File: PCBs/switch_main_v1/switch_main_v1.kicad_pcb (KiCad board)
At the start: 2 copper layers, 15 parts, among them IC1001 TJA1055T_3_2Z, IC1101 MPQ5850GJ-AEC1-Z, J1101 76825-0004, J901 TMJG46945AENL, U1101 TVS2701DRBR, U201 SJA1105QELY, U301 STM32H573RIVx, U401 LT8692SIV-PBF, U402 TPS16416DRCR, U403 LMR34206SC5QRNXRQ1, U501 DP83867CSRGZR, U601 DP83867CSRGZR, U701 DP83867CSRGZR, U801 DP83867CSRGZR

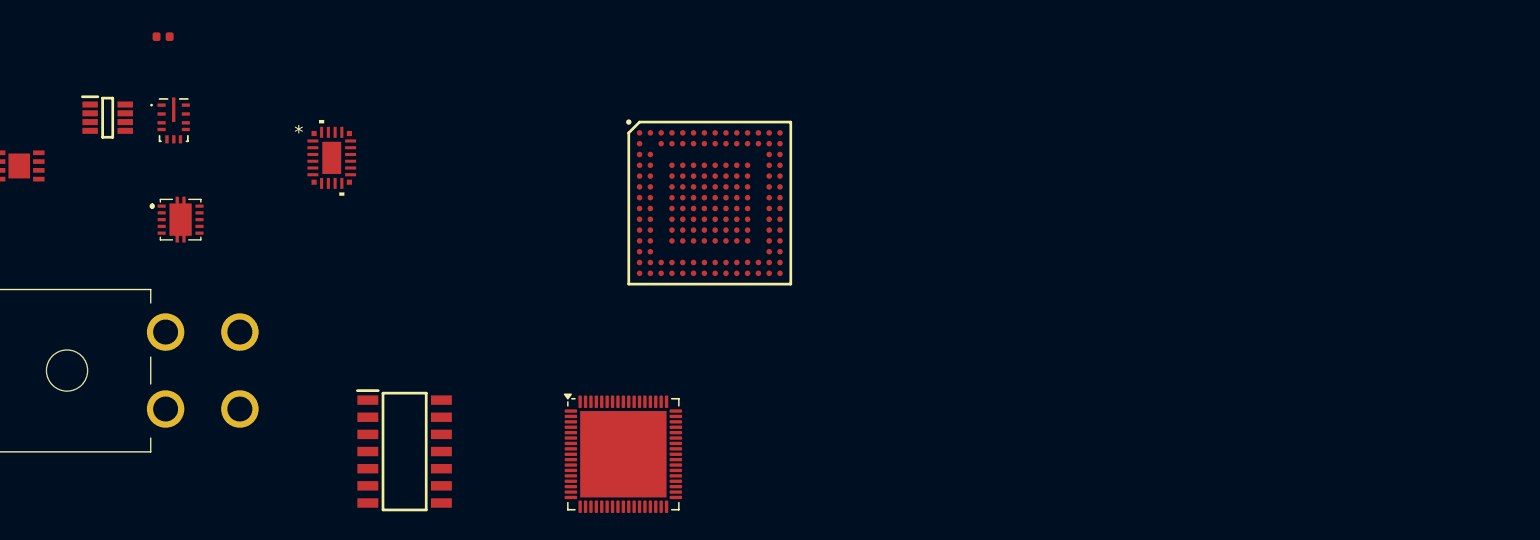
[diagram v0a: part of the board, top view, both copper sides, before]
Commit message: Connectors schematic almost complete
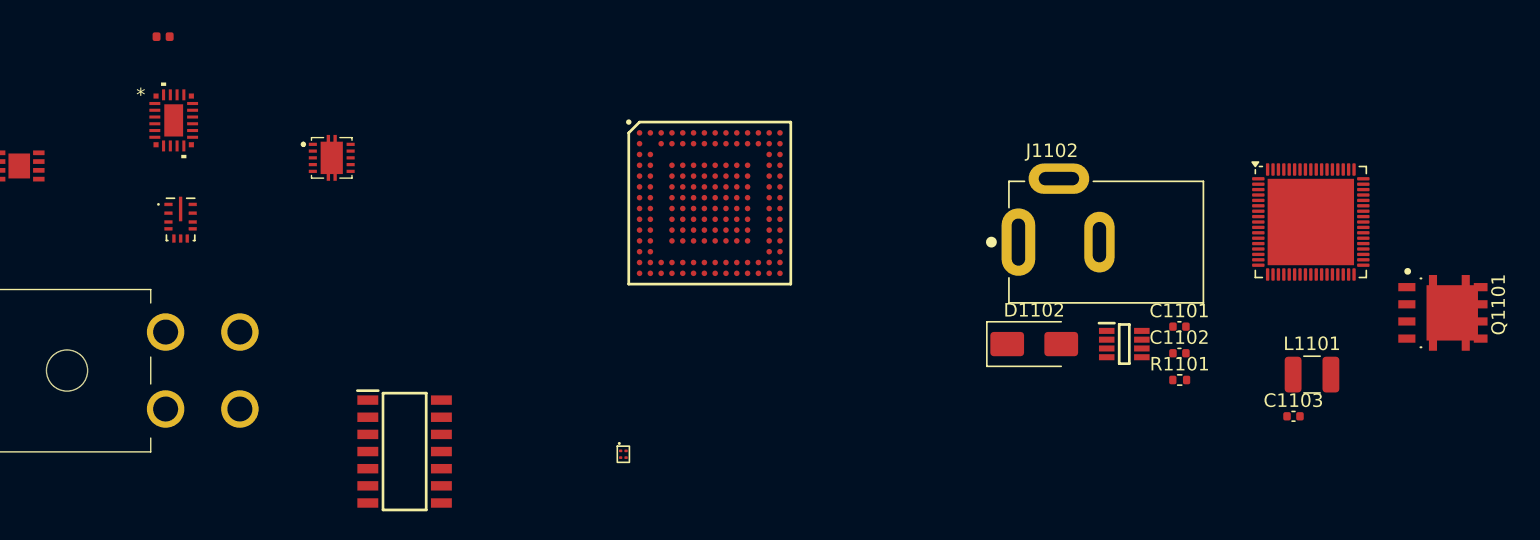
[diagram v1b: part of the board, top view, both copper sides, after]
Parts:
- removed IC1101: MPQ5850GJ-AEC1-Z, switch_footprints:SOT65P280X100-8N
- added C1101: 1u, Capacitor_SMD:C_0402_1005Metric, F.Cu at (206.4, 119.8)
- added C1102: 4u7, Capacitor_SMD:C_0402_1005Metric, F.Cu at (206.4, 121.7)
- added C1103: 10n, Capacitor_SMD:C_0402_1005Metric, F.Cu at (214.8, 126.4)
- added D1102: SK14, Diode_SMD:D_SMA, F.Cu at (195.6, 121.0)
- added J1102: PJ-002AH, switch_footprints:CUI_PJ-002AH, F.Cu at (194.5, 113.5)
- added L1101: BRL3225T680K, Inductor_SMD:L_1210_3225Metric, F.Cu at (216.2, 123.3)
- added Q1101: DMTH6016LPSQ-13, switch_footprints:Diodes_Incorporated-PowerDI5060-8-03_2017-0-MFG, F.Cu at (225.9, 118.7)
- added R1101: 100k, Resistor_SMD:R_0402_1005Metric, F.Cu at (206.4, 123.7)
- added U1102: MPQ5850GJ-AEC1-Z, switch_footprints:SOT65P280X100-8N, F.Cu at (202.3, 121.0)
- added U302: STM32H573RIVx, switch_footprints:QFN-68-1EP_8x8mm_P0.4mm_EP6.4x6.4mm, F.Cu at (216.1, 112.0)
- U301: value STM32H573RIVx -> M24256X-FCU6T_VF; footprint switch_footprints:QFN-68-1EP_8x8mm_P0.4mm_EP6.4x6.4mm -> switch_footprints:BGA4C50P2X2_70X98X33
- U401: value LT8692SIV-PBF -> TPS16416DRCR; footprint switch_footprints:LT8692SIV_PBF -> switch_footprints:TPS74901DRCR
- U402: value TPS16416DRCR -> LMR34206SC5QRNXRQ1; footprint switch_footprints:TPS74901DRCR -> switch_footprints:CONV_LMR33620BRNXT
- U403: value LMR34206SC5QRNXRQ1 -> LT8692SIV-PBF; footprint switch_footprints:CONV_LMR33620BRNXT -> switch_footprints:LT8692SIV_PBF
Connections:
- D1101 pad 2: VDC -> /Connectors/VIN_RAW
- J1101 pad 1: unconnected-(J1101-CANH-Pad1) -> /Connectors/CAN.CANH
- J1101 pad 2: unconnected-(J1101-CANL-Pad2) -> /Connectors/CAN.CANL
- J1101 pad 3: unconnected-(J1101-VSYS-Pad3) -> /Connectors/VIN_RAW
- J1101 pad 4: unconnected-(J1101-GND-Pad4) -> GND
- U1101 pad 1: VDC -> /Connectors/VIN_RAW
- U1101 pad 2: VDC -> /Connectors/VIN_RAW
- U1101 pad 3: VDC -> /Connectors/VIN_RAW
- U1101 pad 4: VDC -> /Connectors/VIN_RAW

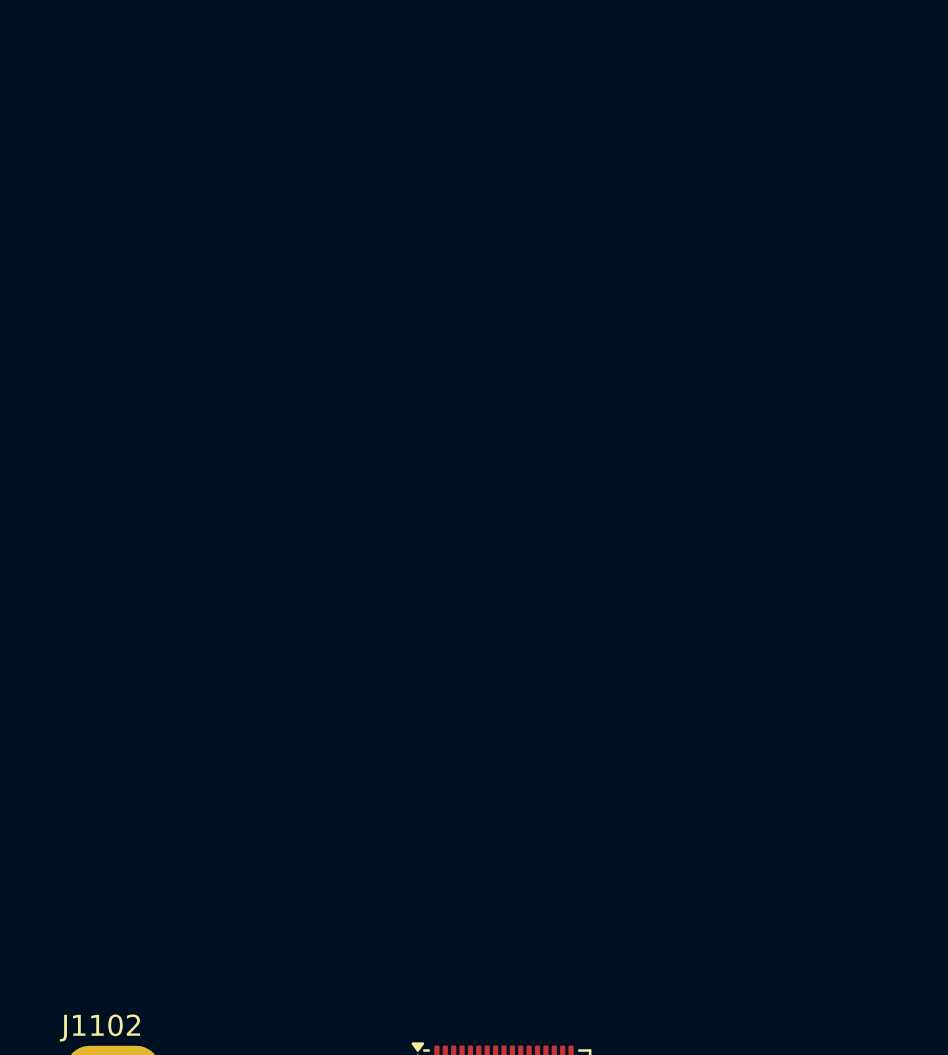
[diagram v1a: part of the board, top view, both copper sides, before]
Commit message: Block diagram layout change
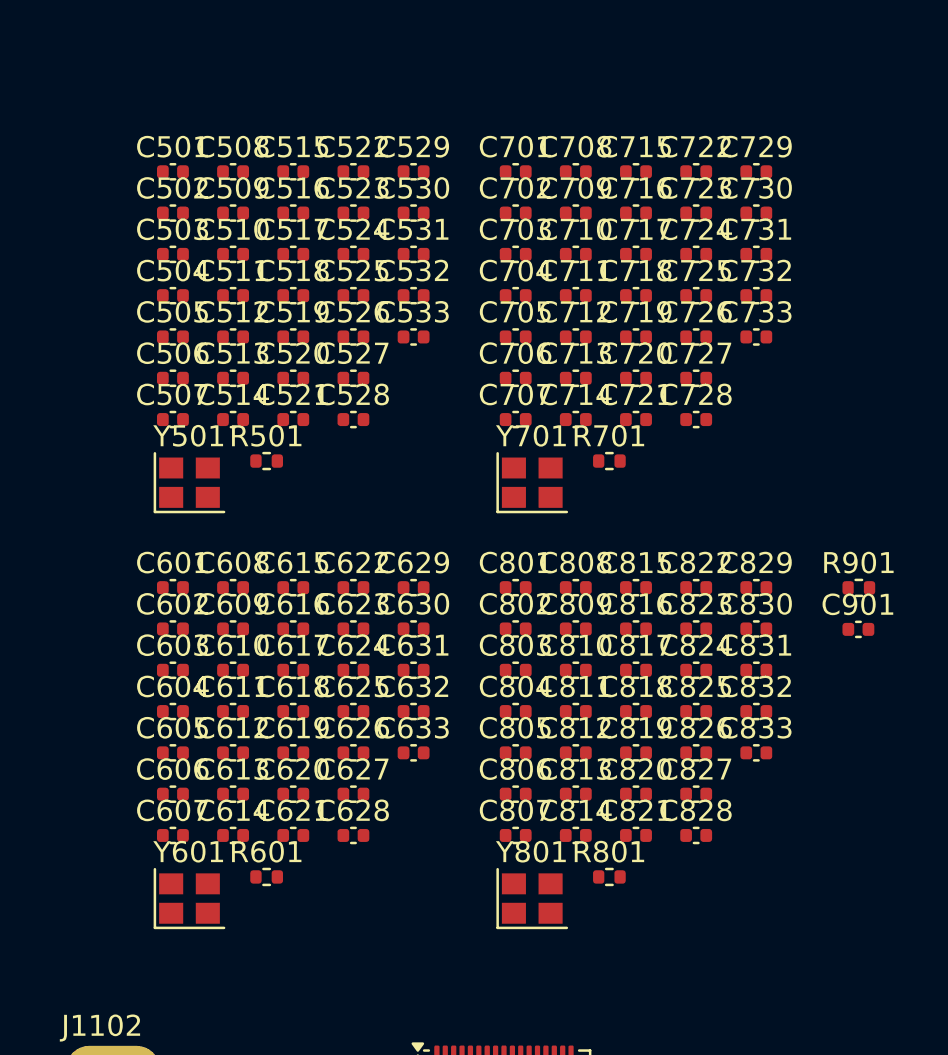
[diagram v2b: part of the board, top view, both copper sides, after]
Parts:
- added C501: 100n, Capacitor_SMD:C_0402_1005Metric, F.Cu at (200.3, 66.0)
- added C502: 100n, Capacitor_SMD:C_0402_1005Metric, F.Cu at (200.3, 67.9)
- added C503: 27p, Capacitor_SMD:C_0402_1005Metric, F.Cu at (200.3, 69.9)
- added C504: 27p, Capacitor_SMD:C_0402_1005Metric, F.Cu at (200.3, 71.9)
- added C505: 27p, Capacitor_SMD:C_0402_1005Metric, F.Cu at (200.3, 73.8)
- added C506: 100n, Capacitor_SMD:C_0402_1005Metric, F.Cu at (200.3, 75.8)
- added C507: 100n, Capacitor_SMD:C_0402_1005Metric, F.Cu at (200.3, 77.8)
- added C508: 100n, Capacitor_SMD:C_0402_1005Metric, F.Cu at (203.2, 66.0)
- added C509: 1u, Capacitor_SMD:C_0402_1005Metric, F.Cu at (203.2, 67.9)
- added C510: 1u, Capacitor_SMD:C_0402_1005Metric, F.Cu at (203.2, 69.9)
- added C511: 1u, Capacitor_SMD:C_0402_1005Metric, F.Cu at (203.2, 71.9)
- added C512: 1u, Capacitor_SMD:C_0402_1005Metric, F.Cu at (203.2, 73.8)
- added C513: 1u, Capacitor_SMD:C_0402_1005Metric, F.Cu at (203.2, 75.8)
- added C514: 10n, Capacitor_SMD:C_0402_1005Metric, F.Cu at (203.2, 77.8)
- added C515: 10u, Capacitor_SMD:C_0402_1005Metric, F.Cu at (206.1, 66.0)
- added C516: 10n, Capacitor_SMD:C_0402_1005Metric, F.Cu at (206.1, 67.9)
- added C517: 10u, Capacitor_SMD:C_0402_1005Metric, F.Cu at (206.1, 69.9)
- added C518: 10n, Capacitor_SMD:C_0402_1005Metric, F.Cu at (206.1, 71.9)
- added C519: 100n, Capacitor_SMD:C_0402_1005Metric, F.Cu at (206.1, 73.8)
- added C520: 100n, Capacitor_SMD:C_0402_1005Metric, F.Cu at (206.1, 75.8)
- added C521: 1u, Capacitor_SMD:C_0402_1005Metric, F.Cu at (206.1, 77.8)
- added C522: 1u, Capacitor_SMD:C_0402_1005Metric, F.Cu at (208.9, 66.0)
- added C523: 10u, Capacitor_SMD:C_0402_1005Metric, F.Cu at (208.9, 67.9)
- added C524: 10n, Capacitor_SMD:C_0402_1005Metric, F.Cu at (208.9, 69.9)
- added C525: 100n, Capacitor_SMD:C_0402_1005Metric, F.Cu at (208.9, 71.9)
- added C526: 100n, Capacitor_SMD:C_0402_1005Metric, F.Cu at (208.9, 73.8)
- added C527: 100n, Capacitor_SMD:C_0402_1005Metric, F.Cu at (208.9, 75.8)
- added C528: 1u, Capacitor_SMD:C_0402_1005Metric, F.Cu at (208.9, 77.8)
- added C529: 1u, Capacitor_SMD:C_0402_1005Metric, F.Cu at (211.8, 66.0)
- added C530: 1u, Capacitor_SMD:C_0402_1005Metric, F.Cu at (211.8, 67.9)
- added C531: 10u, Capacitor_SMD:C_0402_1005Metric, F.Cu at (211.8, 69.9)
- added C532: 100n, Capacitor_SMD:C_0402_1005Metric, F.Cu at (211.8, 71.9)
- added C533: 1u, Capacitor_SMD:C_0402_1005Metric, F.Cu at (211.8, 73.8)
- added C601: 100n, Capacitor_SMD:C_0402_1005Metric, F.Cu at (200.3, 85.8)
- added C602: 100n, Capacitor_SMD:C_0402_1005Metric, F.Cu at (200.3, 87.8)
- added C603: 27p, Capacitor_SMD:C_0402_1005Metric, F.Cu at (200.3, 89.8)
- added C604: 27p, Capacitor_SMD:C_0402_1005Metric, F.Cu at (200.3, 91.7)
- added C605: 27p, Capacitor_SMD:C_0402_1005Metric, F.Cu at (200.3, 93.7)
- added C606: 100n, Capacitor_SMD:C_0402_1005Metric, F.Cu at (200.3, 95.7)
- added C607: 100n, Capacitor_SMD:C_0402_1005Metric, F.Cu at (200.3, 97.6)
- added C608: 100n, Capacitor_SMD:C_0402_1005Metric, F.Cu at (203.2, 85.8)
- added C609: 1u, Capacitor_SMD:C_0402_1005Metric, F.Cu at (203.2, 87.8)
- added C610: 1u, Capacitor_SMD:C_0402_1005Metric, F.Cu at (203.2, 89.8)
- added C611: 1u, Capacitor_SMD:C_0402_1005Metric, F.Cu at (203.2, 91.7)
- added C612: 1u, Capacitor_SMD:C_0402_1005Metric, F.Cu at (203.2, 93.7)
- added C613: 1u, Capacitor_SMD:C_0402_1005Metric, F.Cu at (203.2, 95.7)
- added C614: 10n, Capacitor_SMD:C_0402_1005Metric, F.Cu at (203.2, 97.6)
- added C615: 10u, Capacitor_SMD:C_0402_1005Metric, F.Cu at (206.1, 85.8)
- added C616: 10n, Capacitor_SMD:C_0402_1005Metric, F.Cu at (206.1, 87.8)
- added C617: 10u, Capacitor_SMD:C_0402_1005Metric, F.Cu at (206.1, 89.8)
- added C618: 10n, Capacitor_SMD:C_0402_1005Metric, F.Cu at (206.1, 91.7)
- added C619: 100n, Capacitor_SMD:C_0402_1005Metric, F.Cu at (206.1, 93.7)
- added C620: 100n, Capacitor_SMD:C_0402_1005Metric, F.Cu at (206.1, 95.7)
- added C621: 1u, Capacitor_SMD:C_0402_1005Metric, F.Cu at (206.1, 97.6)
- added C622: 1u, Capacitor_SMD:C_0402_1005Metric, F.Cu at (208.9, 85.8)
- added C623: 10u, Capacitor_SMD:C_0402_1005Metric, F.Cu at (208.9, 87.8)
- added C624: 10n, Capacitor_SMD:C_0402_1005Metric, F.Cu at (208.9, 89.8)
- added C625: 100n, Capacitor_SMD:C_0402_1005Metric, F.Cu at (208.9, 91.7)
- added C626: 100n, Capacitor_SMD:C_0402_1005Metric, F.Cu at (208.9, 93.7)
- added C627: 100n, Capacitor_SMD:C_0402_1005Metric, F.Cu at (208.9, 95.7)
- added C628: 1u, Capacitor_SMD:C_0402_1005Metric, F.Cu at (208.9, 97.6)
- added C629: 1u, Capacitor_SMD:C_0402_1005Metric, F.Cu at (211.8, 85.8)
- added C630: 1u, Capacitor_SMD:C_0402_1005Metric, F.Cu at (211.8, 87.8)
- added C631: 10u, Capacitor_SMD:C_0402_1005Metric, F.Cu at (211.8, 89.8)
- added C632: 100n, Capacitor_SMD:C_0402_1005Metric, F.Cu at (211.8, 91.7)
- added C633: 1u, Capacitor_SMD:C_0402_1005Metric, F.Cu at (211.8, 93.7)
- added C701: 100n, Capacitor_SMD:C_0402_1005Metric, F.Cu at (216.7, 66.0)
- added C702: 100n, Capacitor_SMD:C_0402_1005Metric, F.Cu at (216.7, 67.9)
- added C703: 27p, Capacitor_SMD:C_0402_1005Metric, F.Cu at (216.7, 69.9)
- added C704: 27p, Capacitor_SMD:C_0402_1005Metric, F.Cu at (216.7, 71.9)
- added C705: 27p, Capacitor_SMD:C_0402_1005Metric, F.Cu at (216.7, 73.8)
- added C706: 100n, Capacitor_SMD:C_0402_1005Metric, F.Cu at (216.7, 75.8)
- added C707: 100n, Capacitor_SMD:C_0402_1005Metric, F.Cu at (216.7, 77.8)
- added C708: 100n, Capacitor_SMD:C_0402_1005Metric, F.Cu at (219.5, 66.0)
- added C709: 1u, Capacitor_SMD:C_0402_1005Metric, F.Cu at (219.5, 67.9)
- added C710: 1u, Capacitor_SMD:C_0402_1005Metric, F.Cu at (219.5, 69.9)
- added C711: 1u, Capacitor_SMD:C_0402_1005Metric, F.Cu at (219.5, 71.9)
- added C712: 1u, Capacitor_SMD:C_0402_1005Metric, F.Cu at (219.5, 73.8)
- added C713: 1u, Capacitor_SMD:C_0402_1005Metric, F.Cu at (219.5, 75.8)
- added C714: 10n, Capacitor_SMD:C_0402_1005Metric, F.Cu at (219.5, 77.8)
- added C715: 10u, Capacitor_SMD:C_0402_1005Metric, F.Cu at (222.4, 66.0)
- added C716: 10n, Capacitor_SMD:C_0402_1005Metric, F.Cu at (222.4, 67.9)
- added C717: 10u, Capacitor_SMD:C_0402_1005Metric, F.Cu at (222.4, 69.9)
- added C718: 10n, Capacitor_SMD:C_0402_1005Metric, F.Cu at (222.4, 71.9)
- added C719: 100n, Capacitor_SMD:C_0402_1005Metric, F.Cu at (222.4, 73.8)
- added C720: 100n, Capacitor_SMD:C_0402_1005Metric, F.Cu at (222.4, 75.8)
- added C721: 1u, Capacitor_SMD:C_0402_1005Metric, F.Cu at (222.4, 77.8)
- added C722: 1u, Capacitor_SMD:C_0402_1005Metric, F.Cu at (225.3, 66.0)
- added C723: 10u, Capacitor_SMD:C_0402_1005Metric, F.Cu at (225.3, 67.9)
- added C724: 10n, Capacitor_SMD:C_0402_1005Metric, F.Cu at (225.3, 69.9)
- added C725: 100n, Capacitor_SMD:C_0402_1005Metric, F.Cu at (225.3, 71.9)
- added C726: 100n, Capacitor_SMD:C_0402_1005Metric, F.Cu at (225.3, 73.8)
- added C727: 100n, Capacitor_SMD:C_0402_1005Metric, F.Cu at (225.3, 75.8)
- added C728: 1u, Capacitor_SMD:C_0402_1005Metric, F.Cu at (225.3, 77.8)
- added C729: 1u, Capacitor_SMD:C_0402_1005Metric, F.Cu at (228.2, 66.0)
- added C730: 1u, Capacitor_SMD:C_0402_1005Metric, F.Cu at (228.2, 67.9)
- added C731: 10u, Capacitor_SMD:C_0402_1005Metric, F.Cu at (228.2, 69.9)
- added C732: 100n, Capacitor_SMD:C_0402_1005Metric, F.Cu at (228.2, 71.9)
- added C733: 1u, Capacitor_SMD:C_0402_1005Metric, F.Cu at (228.2, 73.8)
- added C801: 100n, Capacitor_SMD:C_0402_1005Metric, F.Cu at (216.7, 85.8)
- added C802: 100n, Capacitor_SMD:C_0402_1005Metric, F.Cu at (216.7, 87.8)
- added C803: 27p, Capacitor_SMD:C_0402_1005Metric, F.Cu at (216.7, 89.8)
- added C804: 27p, Capacitor_SMD:C_0402_1005Metric, F.Cu at (216.7, 91.7)
- added C805: 27p, Capacitor_SMD:C_0402_1005Metric, F.Cu at (216.7, 93.7)
- added C806: 100n, Capacitor_SMD:C_0402_1005Metric, F.Cu at (216.7, 95.7)
- added C807: 100n, Capacitor_SMD:C_0402_1005Metric, F.Cu at (216.7, 97.6)
- added C808: 100n, Capacitor_SMD:C_0402_1005Metric, F.Cu at (219.5, 85.8)
- added C809: 1u, Capacitor_SMD:C_0402_1005Metric, F.Cu at (219.5, 87.8)
- added C810: 1u, Capacitor_SMD:C_0402_1005Metric, F.Cu at (219.5, 89.8)
- added C811: 1u, Capacitor_SMD:C_0402_1005Metric, F.Cu at (219.5, 91.7)
- added C812: 1u, Capacitor_SMD:C_0402_1005Metric, F.Cu at (219.5, 93.7)
- added C813: 1u, Capacitor_SMD:C_0402_1005Metric, F.Cu at (219.5, 95.7)
- added C814: 10n, Capacitor_SMD:C_0402_1005Metric, F.Cu at (219.5, 97.6)
- added C815: 10u, Capacitor_SMD:C_0402_1005Metric, F.Cu at (222.4, 85.8)
- added C816: 10n, Capacitor_SMD:C_0402_1005Metric, F.Cu at (222.4, 87.8)
- added C817: 10u, Capacitor_SMD:C_0402_1005Metric, F.Cu at (222.4, 89.8)
- added C818: 10n, Capacitor_SMD:C_0402_1005Metric, F.Cu at (222.4, 91.7)
- added C819: 100n, Capacitor_SMD:C_0402_1005Metric, F.Cu at (222.4, 93.7)
- added C820: 100n, Capacitor_SMD:C_0402_1005Metric, F.Cu at (222.4, 95.7)
- added C821: 1u, Capacitor_SMD:C_0402_1005Metric, F.Cu at (222.4, 97.6)
- added C822: 1u, Capacitor_SMD:C_0402_1005Metric, F.Cu at (225.3, 85.8)
- added C823: 10u, Capacitor_SMD:C_0402_1005Metric, F.Cu at (225.3, 87.8)
- added C824: 10n, Capacitor_SMD:C_0402_1005Metric, F.Cu at (225.3, 89.8)
- added C825: 100n, Capacitor_SMD:C_0402_1005Metric, F.Cu at (225.3, 91.7)
- added C826: 100n, Capacitor_SMD:C_0402_1005Metric, F.Cu at (225.3, 93.7)
- added C827: 100n, Capacitor_SMD:C_0402_1005Metric, F.Cu at (225.3, 95.7)
- added C828: 1u, Capacitor_SMD:C_0402_1005Metric, F.Cu at (225.3, 97.6)
- added C829: 1u, Capacitor_SMD:C_0402_1005Metric, F.Cu at (228.2, 85.8)
- added C830: 1u, Capacitor_SMD:C_0402_1005Metric, F.Cu at (228.2, 87.8)
- added C831: 10u, Capacitor_SMD:C_0402_1005Metric, F.Cu at (228.2, 89.8)
- added C832: 100n, Capacitor_SMD:C_0402_1005Metric, F.Cu at (228.2, 91.7)
- added C833: 1u, Capacitor_SMD:C_0402_1005Metric, F.Cu at (228.2, 93.7)
- added C901: C_Small, Capacitor_SMD:C_0402_1005Metric, F.Cu at (233.0, 87.8)
- added R501: 11k, Resistor_SMD:R_0402_1005Metric, F.Cu at (204.8, 79.8)
- added R601: 11k, Resistor_SMD:R_0402_1005Metric, F.Cu at (204.8, 99.6)
- added R701: 11k, Resistor_SMD:R_0402_1005Metric, F.Cu at (221.1, 79.8)
- added R801: 11k, Resistor_SMD:R_0402_1005Metric, F.Cu at (221.1, 99.6)
- added R901: R_Small, Resistor_SMD:R_0402_1005Metric, F.Cu at (233.0, 85.8)
- added Y501: ECS-250-18-36B2-CTY-TR, Crystal:Crystal_SMD_2520-4Pin_2.5x2.0mm, F.Cu at (201.1, 80.8)
- added Y601: ECS-250-18-36B2-CTY-TR, Crystal:Crystal_SMD_2520-4Pin_2.5x2.0mm, F.Cu at (201.1, 100.6)
- added Y701: ECS-250-18-36B2-CTY-TR, Crystal:Crystal_SMD_2520-4Pin_2.5x2.0mm, F.Cu at (217.5, 80.8)
- added Y801: ECS-250-18-36B2-CTY-TR, Crystal:Crystal_SMD_2520-4Pin_2.5x2.0mm, F.Cu at (217.5, 100.6)
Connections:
- J901 pad 15: GND -> Earth
- J901 pad 16: GND -> Earth
- J901 pad 17: GND -> Earth
- J901 pad 18: GND -> Earth
- J901 pad 19: GND -> Earth
- J901 pad 2A: unconnected-(J901-TD1+-Pad2A) -> /ETHERNET_1.TD0_P
- J901 pad 2B: unconnected-(J901-TD1+-Pad2B) -> /ETHERNET_2.TD0_P
- J901 pad 2C: unconnected-(J901-TD1+-Pad2C) -> /ETHERNET_3.TD0_P
- J901 pad 2D: unconnected-(J901-TD1+-Pad2D) -> /ETHERNET_4.TD0_P
- J901 pad 3A: unconnected-(J901-TD1--Pad3A) -> /ETHERNET_1.TD0_N
- J901 pad 3B: unconnected-(J901-TD1--Pad3B) -> /ETHERNET_2.TD0_N
- J901 pad 3C: unconnected-(J901-TD1--Pad3C) -> /ETHERNET_3.TD0_N
- J901 pad 3D: unconnected-(J901-TD1--Pad3D) -> /ETHERNET_4.TD0_N
- J901 pad 4A: unconnected-(J901-TD2+-Pad4A) -> /ETHERNET_1.TD1_P
- J901 pad 4B: unconnected-(J901-TD2+-Pad4B) -> /ETHERNET_2.TD1_P
- J901 pad 4C: unconnected-(J901-TD2+-Pad4C) -> /ETHERNET_3.TD1_P
- J901 pad 4D: unconnected-(J901-TD2+-Pad4D) -> /ETHERNET_4.TD1_P
- J901 pad 5A: unconnected-(J901-TD2--Pad5A) -> /ETHERNET_1.TD1_N
- J901 pad 5B: unconnected-(J901-TD2--Pad5B) -> /ETHERNET_2.TD1_N
- J901 pad 5C: unconnected-(J901-TD2--Pad5C) -> /ETHERNET_3.TD1_N
- J901 pad 5D: unconnected-(J901-TD2--Pad5D) -> /ETHERNET_4.TD1_N
- J901 pad 6A: unconnected-(J901-TD3+-Pad6A) -> /ETHERNET_1.TD2_P
- J901 pad 6B: unconnected-(J901-TD3+-Pad6B) -> /ETHERNET_2.TD2_P
- J901 pad 6C: unconnected-(J901-TD3+-Pad6C) -> /ETHERNET_3.TD2_P
- J901 pad 6D: unconnected-(J901-TD3+-Pad6D) -> /ETHERNET_4.TD2_P
- J901 pad 7A: unconnected-(J901-TD3--Pad7A) -> /ETHERNET_1.TD2_N
- J901 pad 7B: unconnected-(J901-TD3--Pad7B) -> /ETHERNET_2.TD2_N
- J901 pad 7C: unconnected-(J901-TD3--Pad7C) -> /ETHERNET_3.TD2_N
- J901 pad 7D: unconnected-(J901-TD3--Pad7D) -> /ETHERNET_4.TD2_N
- J901 pad 8A: unconnected-(J901-TD4+-Pad8A) -> /ETHERNET_1.TD3_P
- J901 pad 8B: unconnected-(J901-TD4+-Pad8B) -> /ETHERNET_2.TD3_P
- J901 pad 8C: unconnected-(J901-TD4+-Pad8C) -> /ETHERNET_3.TD3_P
- J901 pad 8D: unconnected-(J901-TD4+-Pad8D) -> /ETHERNET_4.TD3_P
- J901 pad 9A: unconnected-(J901-TD4--Pad9A) -> /ETHERNET_1.TD3_N
- J901 pad 9B: unconnected-(J901-TD4--Pad9B) -> /ETHERNET_2.TD3_N
- J901 pad 9C: unconnected-(J901-TD4--Pad9C) -> /ETHERNET_3.TD3_N
- J901 pad 9D: unconnected-(J901-TD4--Pad9D) -> /ETHERNET_4.TD3_N
- U201 pad A11: unconnected-(U201A-MII2_RX_DV/CRS_DV/RX_CTL-PadA11) -> /RGMII_2.RX_CTRL
- U201 pad A12: unconnected-(U201A-MII2_RXD2-PadA12) -> /RGMII_2.RX_D2
- U201 pad A13: unconnected-(U201A-MII2_RXD0-PadA13) -> /RGMII_2.RX_D0
- U201 pad A2: unconnected-(U201A-MII0_TXD0-PadA2) -> /RGMII_0.TX_D0
- U201 pad A4: unconnected-(U201A-MII1_RX_DV/CRS_DV/RX_CTL-PadA4) -> /RGMII_1.RX_CTRL
- U201 pad A5: unconnected-(U201A-MII1_RXD2-PadA5) -> /RGMII_1.RX_D2
- U201 pad A6: unconnected-(U201A-MII1_RXD0-PadA6) -> /RGMII_1.RX_D0
- U201 pad A7: unconnected-(U201A-MII1_TX_CLK/REF_CLK/TXC-PadA7) -> /RGMII_1.TX_CLK
- U201 pad A8: unconnected-(U201A-MII1_TXD3-PadA8) -> /RGMII_1.TX_D3
- U201 pad A9: unconnected-(U201A-MII1_TXD1-PadA9) -> /RGMII_1.TX_D1
- U201 pad B1: unconnected-(U201A-MII0_TXD1-PadB1) -> /RGMII_0.TX_D1
- U201 pad B10: unconnected-(U201A-MII2_RX_ER-PadB10) -> GND
- U201 pad B11: unconnected-(U201A-MII2_RXD3-PadB11) -> /RGMII_2.RX_D3
- U201 pad B12: unconnected-(U201A-MII2_RXD1-PadB12) -> /RGMII_2.RX_D1
- U201 pad B14: unconnected-(U201A-MII2_RX_CLK/RXC-PadB14) -> /RGMII_2.RX_CLK
- U201 pad B3: unconnected-(U201A-MII1_RX_ER-PadB3) -> GND
- U201 pad B4: unconnected-(U201A-MII1_RXD3-PadB4) -> /RGMII_1.RX_D3
- U201 pad B5: unconnected-(U201A-MII1_RXD1-PadB5) -> /RGMII_1.RX_D1
- U201 pad B6: unconnected-(U201A-MII1_RX_CLK/RXC-PadB6) -> /RGMII_1.RX_CLK
- U201 pad B7: unconnected-(U201A-MII1_TTX_EN/TX_CTL-PadB7) -> /RGMII_1.TX_CTRL
- U201 pad B8: unconnected-(U201A-MII1_TXD2-PadB8) -> /RGMII_1.TX_D2
- U201 pad B9: unconnected-(U201A-MII1_TXD0-PadB9) -> /RGMII_1.TX_D0
- U201 pad C1: unconnected-(U201A-MII0_TXD3-PadC1) -> /RGMII_0.TX_D3
- U201 pad C13: unconnected-(U201A-MII2_TX_EN/TX_CTL-PadC13) -> /RGMII_2.TX_CTRL
- U201 pad C14: unconnected-(U201A-MII2_TX_CLK/REF_CLK/TXC-PadC14) -> /RGMII_2.TX_CLK
- U201 pad C2: unconnected-(U201A-MII0_TXD2-PadC2) -> /RGMII_0.TX_D2
- U201 pad D1: unconnected-(U201A-MII0_TX_CLK/REF_CLK/TXC-PadD1) -> /RGMII_0.TX_CLK
- U201 pad D10: unconnected-(U201B-VDDIO_MII2_1-PadD10) -> +2V5
- U201 pad D11: unconnected-(U201B-VDDIO_MII2_2-PadD11) -> +2V5
- U201 pad D13: unconnected-(U201A-MII2_TXD2-PadD13) -> /RGMII_2.TX_D2
- U201 pad D14: unconnected-(U201A-MII2_TXD3-PadD14) -> /RGMII_2.TX_D3
- U201 pad D2: unconnected-(U201A-MII0_TX_EN/TX_CTL-PadD2) -> /RGMII_0.TX_CTRL
- U201 pad D4: unconnected-(U201B-VDDIO_MII0_1-PadD4) -> +2V5
- U201 pad D5: unconnected-(U201B-VDDIO_MII1_1-PadD5) -> +2V5
- U201 pad D6: unconnected-(U201B-VDD_CORE_1-PadD6) -> +1V2
- U201 pad D7: unconnected-(U201B-VDDIO_MII1_2-PadD7) -> +2V5
- U201 pad D8: unconnected-(U201B-VDDIO_MII1_3-PadD8) -> +2V5
- U201 pad D9: unconnected-(U201B-VDD_CORE_2-PadD9) -> +1V2
- U201 pad E1: unconnected-(U201A-MII0_RXD0-PadE1) -> /RGMII_0.RX_D0
- U201 pad E11: unconnected-(U201B-VDDIO_MII2_3-PadE11) -> +2V5
- U201 pad E13: unconnected-(U201A-MII2_TXD0-PadE13) -> /RGMII_2.TX_D0
- U201 pad E14: unconnected-(U201A-MII2_TXD1-PadE14) -> /RGMII_2.TX_D1
- U201 pad E2: unconnected-(U201A-MII0_RX_CLK/RXC-PadE2) -> /RGMII_0.RX_CLK
- U201 pad E4: unconnected-(U201B-VDDIO_MII0_2-PadE4) -> +2V5
- U201 pad F1: unconnected-(U201A-MII0_RXD2-PadF1) -> /RGMII_0.RX_D2
- U201 pad F11: unconnected-(U201B-VDD_CORE_4-PadF11) -> +1V2
- U201 pad F13: unconnected-(U201A-MII3_RX_ER-PadF13) -> GND
- U201 pad F2: unconnected-(U201A-MII0_RXD1-PadF2) -> /RGMII_0.RX_D1
- U201 pad F4: unconnected-(U201B-VDD_CORE_3-PadF4) -> +1V2
- U201 pad G1: unconnected-(U201A-MII0_RX_DV/CRS_DV/RX_CTL-PadG1) -> /RGMII_0.RX_CTRL
- U201 pad G11: unconnected-(U201B-VDDIO_MII3_1-PadG11) -> +2V5
- U201 pad G13: unconnected-(U201A-MII3_RXD3-PadG13) -> /RGMII_3.RX_D3
- U201 pad G14: unconnected-(U201A-MII3_RX_DV/CRS_DV/RX_CTL-PadG14) -> /RGMII_3.RX_CTRL
- U201 pad G2: unconnected-(U201A-MII0_RXD3-PadG2) -> /RGMII_0.RX_D3
- U201 pad G4: unconnected-(U201B-VDDIO_MII0_3-PadG4) -> +2V5
- U201 pad H1: unconnected-(U201A-CLK_OUT-PadH1) -> /PHY_1_CLK
- U201 pad H11: unconnected-(U201B-VDDIO_MII3_2-PadH11) -> +2V5
- U201 pad H13: unconnected-(U201A-MII3_RXD1-PadH13) -> /RGMII_3.RX_D1
- U201 pad H14: unconnected-(U201A-MII3_RXD2-PadH14) -> /RGMII_3.RX_D2
- U201 pad H2: unconnected-(U201A-MII0_RX_ER-PadH2) -> GND
- U201 pad H4: unconnected-(U201B-VDDIO_CLO-PadH4) -> +2V5
- U201 pad J11: unconnected-(U201B-VDD_CORE_6-PadJ11) -> +1V2
- U201 pad J13: unconnected-(U201A-MII3_RX_CLK/RXC-PadJ13) -> /RGMII_3.RX_CLK
- U201 pad J14: unconnected-(U201A-MII3_RXD0-PadJ14) -> /RGMII_3.RX_D0
- U201 pad J4: unconnected-(U201B-VDD_CORE_5-PadJ4) -> +1V2
- U201 pad K11: unconnected-(U201B-VDDIO_MII3_3-PadK11) -> +2V5
- U201 pad K13: unconnected-(U201A-MII3_TX_EN/TX_CTL-PadK13) -> /RGMII_3.TX_CTRL
- U201 pad K14: unconnected-(U201A-MII3_TX_CLK/REF_CLK/TXC-PadK14) -> /RGMII_3.TX_CLK
- U201 pad L10: unconnected-(U201B-VDDIO_MII4_2-PadL10) -> +2V5
- U201 pad L11: unconnected-(U201B-VDDIO_MII4_3-PadL11) -> +2V5
- U201 pad L13: unconnected-(U201A-MII3_TXD2-PadL13) -> /RGMII_3.TX_D2
- U201 pad L14: unconnected-(U201A-MII3_TXD3-PadL14) -> /RGMII_3.TX_D3
- U201 pad L5: unconnected-(U201B-VDDIO_HOST-PadL5) -> +2V5
- U201 pad L6: unconnected-(U201B-VDD_CORE_7-PadL6) -> +1V2
- U201 pad L8: unconnected-(U201B-VDDIO_MII4_1-PadL8) -> +2V5
- U201 pad L9: unconnected-(U201B-VDD_CORE_8-PadL9) -> +1V2
- U201 pad M13: unconnected-(U201A-MII3_TXD0-PadM13) -> /RGMII_3.TX_D0
- U201 pad M14: unconnected-(U201A-MII3_TXD1-PadM14) -> /RGMII_3.TX_D1
- U201 pad N10: unconnected-(U201A-MII4_RXD0-PadN10) -> /RMII.RX_D0
- U201 pad N11: unconnected-(U201A-MII4_RXD2-PadN11) -> GND
- U201 pad N12: unconnected-(U201A-MII4_RX_DV/CRS_DV/RX_CTL-PadN12) -> /RMII.CRS_DV
- U201 pad N4: unconnected-(U201A-PTP_CLK-PadN4) -> /PTP_CLK
- U201 pad N5: unconnected-(U201A-SDI-PadN5) -> /Switch/SPI.MOSI
- U201 pad N6: unconnected-(U201A-SS_N-PadN6) -> /Switch/SPI.CS
- U201 pad N7: unconnected-(U201A-MII4_TXD1-PadN7) -> /RMII.TX_D1
- U201 pad N9: unconnected-(U201A-MII4_TX_CLK/REF_CLK/TXC-PadN9) -> /RMII.REF_CLK
- U201 pad P10: unconnected-(U201A-MII4_RX_CLK/RXC-PadP10) -> GND
- U201 pad P11: unconnected-(U201A-MII4_RXD1-PadP11) -> /RMII.RX_D1
- U201 pad P12: unconnected-(U201A-MII4_RXD3-PadP12) -> GND
- U201 pad P13: unconnected-(U201A-MII4_RX_ER-PadP13) -> GND
- U201 pad P3: unconnected-(U201A-RST_N-PadP3) -> /Switch/RST
- U201 pad P4: unconnected-(U201A-SDO-PadP4) -> /Switch/SPI.MISO
- U201 pad P5: unconnected-(U201A-SCK-PadP5) -> /Switch/SPI.SCK
- U201 pad P7: unconnected-(U201A-MII4_TXD0-PadP7) -> /RMII.TX_D0
- U201 pad P9: unconnected-(U201A-MII4_TX_EN/TX_CTL-PadP9) -> /RMII.TX_EN
- U302 pad 59: /MCU/ETH_PPS_OUT -> /PTP_CLK
- U402 pad 9: unconnected-(U402-EN-Pad9) -> /Power/5V0_EN
- U501 pad 1: unconnected-(U501-TD_P_A-Pad1) -> /ETHERNET_1.TD0_P
- U501 pad 10: unconnected-(U501-TD_P_D-Pad10) -> /ETHERNET_1.TD3_P
- U501 pad 11: unconnected-(U501-TD_M_D-Pad11) -> /ETHERNET_1.TD3_N
- U501 pad 12: unconnected-(U501-RBIAS-Pad12) -> /PHY 1/RBIAS
- U501 pad 13: unconnected-(U501-VDDA1P8_1-Pad13) -> +1V8
- U501 pad 14: unconnected-(U501-XO-Pad14) -> /PHY 1/XO
- U501 pad 15: unconnected-(U501-XI-Pad15) -> /PHY 1/XI
- U501 pad 16: unconnected-(U501-MDC-Pad16) -> /SMI.MDIO
- U501 pad 17: unconnected-(U501-MDIO-Pad17) -> /SMI.MDC
- U501 pad 18: unconnected-(U501-CLK_OUT-Pad18) -> /PHY_2_CLK
- U501 pad 19: unconnected-(U501-VDDIO_1-Pad19) -> +2V5
- U501 pad 2: unconnected-(U501-TD_M_A-Pad2) -> /ETHERNET_1.TD0_N
- U501 pad 24: unconnected-(U501-VDD1P0_2-Pad24) -> +1V0
- U501 pad 25: unconnected-(U501-TX_D3-Pad25) -> /RGMII_0.TX_D3
- U501 pad 26: unconnected-(U501-TX_D2-Pad26) -> /RGMII_0.TX_D2
- U501 pad 27: unconnected-(U501-TX_D1/SGMII_SIP-Pad27) -> /RGMII_0.TX_D1
- U501 pad 28: unconnected-(U501-TX_D0/SGMII_SIN-Pad28) -> /RGMII_0.TX_D0
- U501 pad 29: unconnected-(U501-GTX_CLK-Pad29) -> /RGMII_0.TX_CLK
- U501 pad 3: unconnected-(U501-VDDA2P5_1-Pad3) -> +2V5
- U501 pad 30: unconnected-(U501-VDDIO_2-Pad30) -> +2V5
- U501 pad 31: unconnected-(U501-VDD1P0_3-Pad31) -> +1V0
- U501 pad 32: unconnected-(U501-RX_CLK-Pad32) -> /RGMII_0.RX_CLK
- U501 pad 33: unconnected-(U501-RX_D0/SGMII_COP-Pad33) -> /RGMII_0.RX_D0
- U501 pad 34: unconnected-(U501-RX_D1/SGMII_CON-Pad34) -> /RGMII_0.RX_D1
- U501 pad 35: unconnected-(U501-RX_D2/SGMII_SOP-Pad35) -> /RGMII_0.RX_D2
- U501 pad 36: unconnected-(U501-RX_D3/SGMII_SON-Pad36) -> /RGMII_0.RX_D3
- U501 pad 37: unconnected-(U501-TX_CTRL-Pad37) -> /RGMII_0.TX_CTRL
- U501 pad 38: unconnected-(U501-RX_CTRL-Pad38) -> /RGMII_0.RX_CTRL
- U501 pad 4: unconnected-(U501-TD_P_B-Pad4) -> /ETHERNET_1.TD1_P
- U501 pad 41: unconnected-(U501-VDDIO_3-Pad41) -> +2V5
- U501 pad 42: unconnected-(U501-VDD1P0_4-Pad42) -> +1V0
- U501 pad 48: unconnected-(U501-VDDA1P8_2-Pad48) -> +1V8
- U501 pad 49: unconnected-(U501-GND-Pad49) -> GND
- U501 pad 5: unconnected-(U501-TD_M_B-Pad5) -> /ETHERNET_1.TD1_N
- U501 pad 6: unconnected-(U501-VDD1P0_1-Pad6) -> +1V0
- U501 pad 7: unconnected-(U501-TD_P_C-Pad7) -> /ETHERNET_1.TD2_P
- U501 pad 8: unconnected-(U501-TD_M_C-Pad8) -> /ETHERNET_1.TD2_N
- U501 pad 9: unconnected-(U501-VDDA2P5_2-Pad9) -> +2V5
- U601 pad 1: unconnected-(U601-TD_P_A-Pad1) -> /ETHERNET_2.TD0_P
- U601 pad 10: unconnected-(U601-TD_P_D-Pad10) -> /ETHERNET_2.TD3_P
- U601 pad 11: unconnected-(U601-TD_M_D-Pad11) -> /ETHERNET_2.TD3_N
- U601 pad 12: unconnected-(U601-RBIAS-Pad12) -> /PHY 2/RBIAS
- U601 pad 13: unconnected-(U601-VDDA1P8_1-Pad13) -> +1V8
- U601 pad 14: unconnected-(U601-XO-Pad14) -> /PHY 2/XO
- U601 pad 15: unconnected-(U601-XI-Pad15) -> /PHY 2/XI
- U601 pad 16: unconnected-(U601-MDC-Pad16) -> /SMI.MDIO
- U601 pad 17: unconnected-(U601-MDIO-Pad17) -> /SMI.MDC
- U601 pad 18: unconnected-(U601-CLK_OUT-Pad18) -> /PHY_3_CLK
- U601 pad 19: unconnected-(U601-VDDIO_1-Pad19) -> +2V5
- U601 pad 2: unconnected-(U601-TD_M_A-Pad2) -> /ETHERNET_2.TD0_N
- U601 pad 24: unconnected-(U601-VDD1P0_2-Pad24) -> +1V0
- U601 pad 25: unconnected-(U601-TX_D3-Pad25) -> /RGMII_1.TX_D3
- U601 pad 26: unconnected-(U601-TX_D2-Pad26) -> /RGMII_1.TX_D2
- U601 pad 27: unconnected-(U601-TX_D1/SGMII_SIP-Pad27) -> /RGMII_1.TX_D1
- U601 pad 28: unconnected-(U601-TX_D0/SGMII_SIN-Pad28) -> /RGMII_1.TX_D0
- U601 pad 29: unconnected-(U601-GTX_CLK-Pad29) -> /RGMII_1.TX_CLK
- U601 pad 3: unconnected-(U601-VDDA2P5_1-Pad3) -> +2V5
- U601 pad 30: unconnected-(U601-VDDIO_2-Pad30) -> +2V5
- U601 pad 31: unconnected-(U601-VDD1P0_3-Pad31) -> +1V0
- U601 pad 32: unconnected-(U601-RX_CLK-Pad32) -> /RGMII_1.RX_CLK
- U601 pad 33: unconnected-(U601-RX_D0/SGMII_COP-Pad33) -> /RGMII_1.RX_D0
- U601 pad 34: unconnected-(U601-RX_D1/SGMII_CON-Pad34) -> /RGMII_1.RX_D1
- U601 pad 35: unconnected-(U601-RX_D2/SGMII_SOP-Pad35) -> /RGMII_1.RX_D2
- U601 pad 36: unconnected-(U601-RX_D3/SGMII_SON-Pad36) -> /RGMII_1.RX_D3
- U601 pad 37: unconnected-(U601-TX_CTRL-Pad37) -> /RGMII_1.TX_CTRL
- U601 pad 38: unconnected-(U601-RX_CTRL-Pad38) -> /RGMII_1.RX_CTRL
- U601 pad 4: unconnected-(U601-TD_P_B-Pad4) -> /ETHERNET_2.TD1_P
- U601 pad 41: unconnected-(U601-VDDIO_3-Pad41) -> +2V5
- U601 pad 42: unconnected-(U601-VDD1P0_4-Pad42) -> +1V0
- U601 pad 48: unconnected-(U601-VDDA1P8_2-Pad48) -> +1V8
- U601 pad 49: unconnected-(U601-GND-Pad49) -> GND
- U601 pad 5: unconnected-(U601-TD_M_B-Pad5) -> /ETHERNET_2.TD1_N
- U601 pad 6: unconnected-(U601-VDD1P0_1-Pad6) -> +1V0
- U601 pad 7: unconnected-(U601-TD_P_C-Pad7) -> /ETHERNET_2.TD2_P
- U601 pad 8: unconnected-(U601-TD_M_C-Pad8) -> /ETHERNET_2.TD2_N
- U601 pad 9: unconnected-(U601-VDDA2P5_2-Pad9) -> +2V5
- U701 pad 1: unconnected-(U701-TD_P_A-Pad1) -> /ETHERNET_3.TD0_P
- U701 pad 10: unconnected-(U701-TD_P_D-Pad10) -> /ETHERNET_3.TD3_P
- U701 pad 11: unconnected-(U701-TD_M_D-Pad11) -> /ETHERNET_3.TD3_N
- U701 pad 12: unconnected-(U701-RBIAS-Pad12) -> /PHY 3/RBIAS
- U701 pad 13: unconnected-(U701-VDDA1P8_1-Pad13) -> +1V8
- U701 pad 14: unconnected-(U701-XO-Pad14) -> /PHY 3/XO
- U701 pad 15: unconnected-(U701-XI-Pad15) -> /PHY 3/XI
- U701 pad 16: unconnected-(U701-MDC-Pad16) -> /SMI.MDIO
- U701 pad 17: unconnected-(U701-MDIO-Pad17) -> /SMI.MDC
- U701 pad 18: unconnected-(U701-CLK_OUT-Pad18) -> /PHY_4_CLK
- U701 pad 19: unconnected-(U701-VDDIO_1-Pad19) -> +2V5
- U701 pad 2: unconnected-(U701-TD_M_A-Pad2) -> /ETHERNET_3.TD0_N
- U701 pad 24: unconnected-(U701-VDD1P0_2-Pad24) -> +1V0
- U701 pad 25: unconnected-(U701-TX_D3-Pad25) -> /RGMII_2.TX_D3
- U701 pad 26: unconnected-(U701-TX_D2-Pad26) -> /RGMII_2.TX_D2
- U701 pad 27: unconnected-(U701-TX_D1/SGMII_SIP-Pad27) -> /RGMII_2.TX_D1
- U701 pad 28: unconnected-(U701-TX_D0/SGMII_SIN-Pad28) -> /RGMII_2.TX_D0
- U701 pad 29: unconnected-(U701-GTX_CLK-Pad29) -> /RGMII_2.TX_CLK
- U701 pad 3: unconnected-(U701-VDDA2P5_1-Pad3) -> +2V5
- U701 pad 30: unconnected-(U701-VDDIO_2-Pad30) -> +2V5
- U701 pad 31: unconnected-(U701-VDD1P0_3-Pad31) -> +1V0
- U701 pad 32: unconnected-(U701-RX_CLK-Pad32) -> /RGMII_2.RX_CLK
- U701 pad 33: unconnected-(U701-RX_D0/SGMII_COP-Pad33) -> /RGMII_2.RX_D0
- U701 pad 34: unconnected-(U701-RX_D1/SGMII_CON-Pad34) -> /RGMII_2.RX_D1
- U701 pad 35: unconnected-(U701-RX_D2/SGMII_SOP-Pad35) -> /RGMII_2.RX_D2
- U701 pad 36: unconnected-(U701-RX_D3/SGMII_SON-Pad36) -> /RGMII_2.RX_D3
- U701 pad 37: unconnected-(U701-TX_CTRL-Pad37) -> /RGMII_2.TX_CTRL
- U701 pad 38: unconnected-(U701-RX_CTRL-Pad38) -> /RGMII_2.RX_CTRL
- U701 pad 4: unconnected-(U701-TD_P_B-Pad4) -> /ETHERNET_3.TD1_P
- U701 pad 41: unconnected-(U701-VDDIO_3-Pad41) -> +2V5
- U701 pad 42: unconnected-(U701-VDD1P0_4-Pad42) -> +1V0
- U701 pad 48: unconnected-(U701-VDDA1P8_2-Pad48) -> +1V8
- U701 pad 49: unconnected-(U701-GND-Pad49) -> GND
- U701 pad 5: unconnected-(U701-TD_M_B-Pad5) -> /ETHERNET_3.TD1_N
- U701 pad 6: unconnected-(U701-VDD1P0_1-Pad6) -> +1V0
- U701 pad 7: unconnected-(U701-TD_P_C-Pad7) -> /ETHERNET_3.TD2_P
- U701 pad 8: unconnected-(U701-TD_M_C-Pad8) -> /ETHERNET_3.TD2_N
- U701 pad 9: unconnected-(U701-VDDA2P5_2-Pad9) -> +2V5
- U801 pad 1: unconnected-(U801-TD_P_A-Pad1) -> /ETHERNET_4.TD0_P
- U801 pad 10: unconnected-(U801-TD_P_D-Pad10) -> /ETHERNET_4.TD3_P
- U801 pad 11: unconnected-(U801-TD_M_D-Pad11) -> /ETHERNET_4.TD3_N
- U801 pad 12: unconnected-(U801-RBIAS-Pad12) -> /PHY 4/RBIAS
- U801 pad 13: unconnected-(U801-VDDA1P8_1-Pad13) -> +1V8
- U801 pad 14: unconnected-(U801-XO-Pad14) -> /PHY 4/XO
- U801 pad 15: unconnected-(U801-XI-Pad15) -> /PHY 4/XI
- U801 pad 16: unconnected-(U801-MDC-Pad16) -> /SMI.MDIO
- U801 pad 17: unconnected-(U801-MDIO-Pad17) -> /SMI.MDC
- U801 pad 18: unconnected-(U801-CLK_OUT-Pad18) -> /PHY 4/CLK_OUT
- U801 pad 19: unconnected-(U801-VDDIO_1-Pad19) -> +2V5
- U801 pad 2: unconnected-(U801-TD_M_A-Pad2) -> /ETHERNET_4.TD0_N
- U801 pad 24: unconnected-(U801-VDD1P0_2-Pad24) -> +1V0
- U801 pad 25: unconnected-(U801-TX_D3-Pad25) -> /RGMII_3.TX_D3
- U801 pad 26: unconnected-(U801-TX_D2-Pad26) -> /RGMII_3.TX_D2
- U801 pad 27: unconnected-(U801-TX_D1/SGMII_SIP-Pad27) -> /RGMII_3.TX_D1
- U801 pad 28: unconnected-(U801-TX_D0/SGMII_SIN-Pad28) -> /RGMII_3.TX_D0
- U801 pad 29: unconnected-(U801-GTX_CLK-Pad29) -> /RGMII_3.TX_CLK
- U801 pad 3: unconnected-(U801-VDDA2P5_1-Pad3) -> +2V5
- U801 pad 30: unconnected-(U801-VDDIO_2-Pad30) -> +2V5
- U801 pad 31: unconnected-(U801-VDD1P0_3-Pad31) -> +1V0
- U801 pad 32: unconnected-(U801-RX_CLK-Pad32) -> /RGMII_3.RX_CLK
- U801 pad 33: unconnected-(U801-RX_D0/SGMII_COP-Pad33) -> /RGMII_3.RX_D0
- U801 pad 34: unconnected-(U801-RX_D1/SGMII_CON-Pad34) -> /RGMII_3.RX_D1
- U801 pad 35: unconnected-(U801-RX_D2/SGMII_SOP-Pad35) -> /RGMII_3.RX_D2
- U801 pad 36: unconnected-(U801-RX_D3/SGMII_SON-Pad36) -> /RGMII_3.RX_D3
- U801 pad 37: unconnected-(U801-TX_CTRL-Pad37) -> /RGMII_3.TX_CTRL
- U801 pad 38: unconnected-(U801-RX_CTRL-Pad38) -> /RGMII_3.RX_CTRL
- U801 pad 4: unconnected-(U801-TD_P_B-Pad4) -> /ETHERNET_4.TD1_P
- U801 pad 41: unconnected-(U801-VDDIO_3-Pad41) -> +2V5
- U801 pad 42: unconnected-(U801-VDD1P0_4-Pad42) -> +1V0
- U801 pad 48: unconnected-(U801-VDDA1P8_2-Pad48) -> +1V8
- U801 pad 49: unconnected-(U801-GND-Pad49) -> GND
- U801 pad 5: unconnected-(U801-TD_M_B-Pad5) -> /ETHERNET_4.TD1_N
- U801 pad 6: unconnected-(U801-VDD1P0_1-Pad6) -> +1V0
- U801 pad 7: unconnected-(U801-TD_P_C-Pad7) -> /ETHERNET_4.TD2_P
- U801 pad 8: unconnected-(U801-TD_M_C-Pad8) -> /ETHERNET_4.TD2_N
- U801 pad 9: unconnected-(U801-VDDA2P5_2-Pad9) -> +2V5
